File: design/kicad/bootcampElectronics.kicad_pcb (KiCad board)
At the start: 2 copper layers, 35.7 x 23.9 mm, 17 parts, among them J3 FTDI, SW1 SW_Push, Y1 16MHz

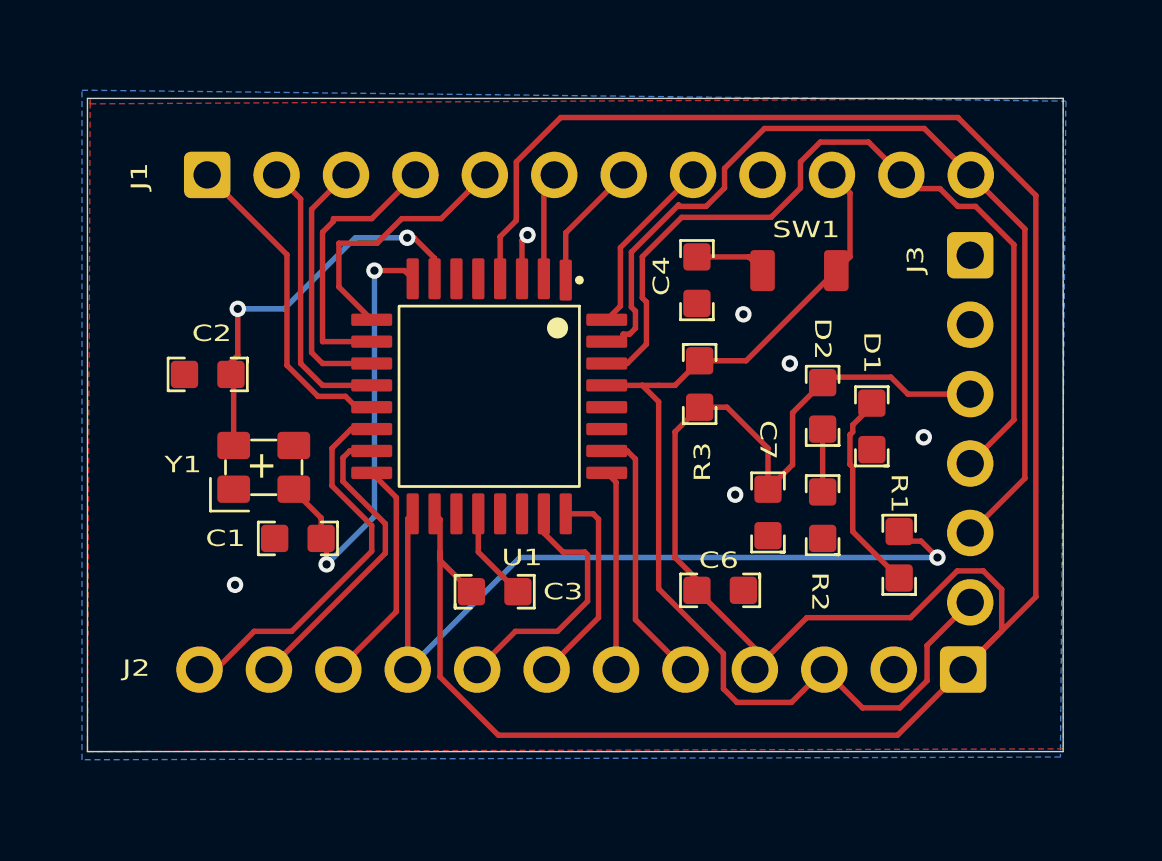
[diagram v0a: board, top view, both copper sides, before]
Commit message: Fixed PCB and footprints/datasheets changed
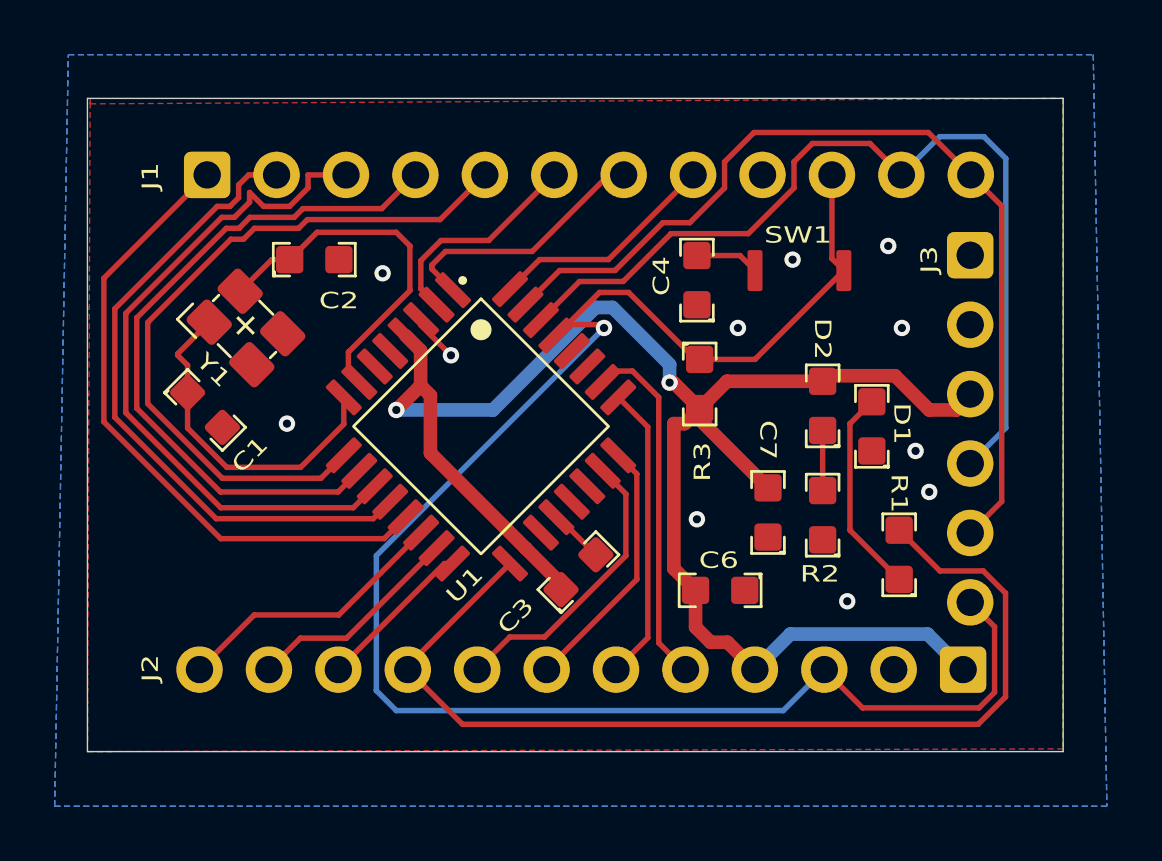
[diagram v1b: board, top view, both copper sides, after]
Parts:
- moved C1 5.80 mm to (152.0, 97.0), turned to 135 degrees
- moved C2 5.73 mm to (156.0, 91.5), turned to 180 degrees
- moved Y1 5.14 mm to (153.5, 94.0), turned to -45 degrees
- moved C3 3.15 mm to (165.7, 102.9), turned to -135 degrees
- moved U1 1.14 mm to (162.1, 97.6), turned to -45 degrees
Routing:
- net RAW: track 113.7 -> 63.1 mm, vias 0 -> 2
- net DTR: track 39.1 -> 63.9 mm, vias 0 -> 1
- net D5: track 9.67 -> 26.2 mm
- net D7: track 9.39 -> 25.6 mm
- net D6: track 10.1 -> 25.4 mm
- net D8: track 10.2 -> 24.1 mm
- net D9: track 11.9 -> 23.7 mm
- net SCK: track 28.6 -> 37.2 mm, vias 1 -> 0
- net D3: track 4.73 -> 9.62 mm
- net D4: track 3.96 -> 8.03 mm
- net D10: track 14.2 -> 10.2 mm
- net Net-(U1-XTAL2/PB7): track 16.2 -> 12.4 mm, vias 2 -> 0
- net A2: track 7.34 -> 10.9 mm
- net A3: track 9.63 -> 13.0 mm
- net MOSI: track 11.3 -> 7.97 mm
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
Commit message: finished
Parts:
- added G***: LOGO, footprints:br, F.Cu at (150.6, 102.1)
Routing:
- net D7: track 25.6 -> 24.1 mm
- net DTR: track 63.9 -> 62.6 mm
- net D6: track 25.4 -> 24.5 mm
- net D5: track 26.2 -> 25.3 mm
- net D8: track 24.1 -> 23.2 mm
- net TXO: track 34.1 -> 33.3 mm
- net D9: track 23.7 -> 23.0 mm
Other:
- board text added: "A0"
- board text added: "A1"
- board text added: "A2"
- board text added: "A3"
- board text added: "D10"
- board text added: "D2"
- board text added: "D3"
- board text added: "D4"
- board text added: "D5"
- board text added: "D6"
- board text added: "D7"
- board text added: "D8"
- board text added: "D9"
- board text added: "DTR"
- board text added: "GND"
- board text added: "MISO"
- board text added: "MOSI"
- board text added: "RAW"
- board text added: "RXI"
- board text added: "SCK"
- board text added: "TXO"
